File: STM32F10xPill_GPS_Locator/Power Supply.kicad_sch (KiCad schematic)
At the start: 42 parts, among them J3 Conn_01x02, Q1 2301D, U2 MCP73871T-2CCI/ML, U3 TPS61022RWUR

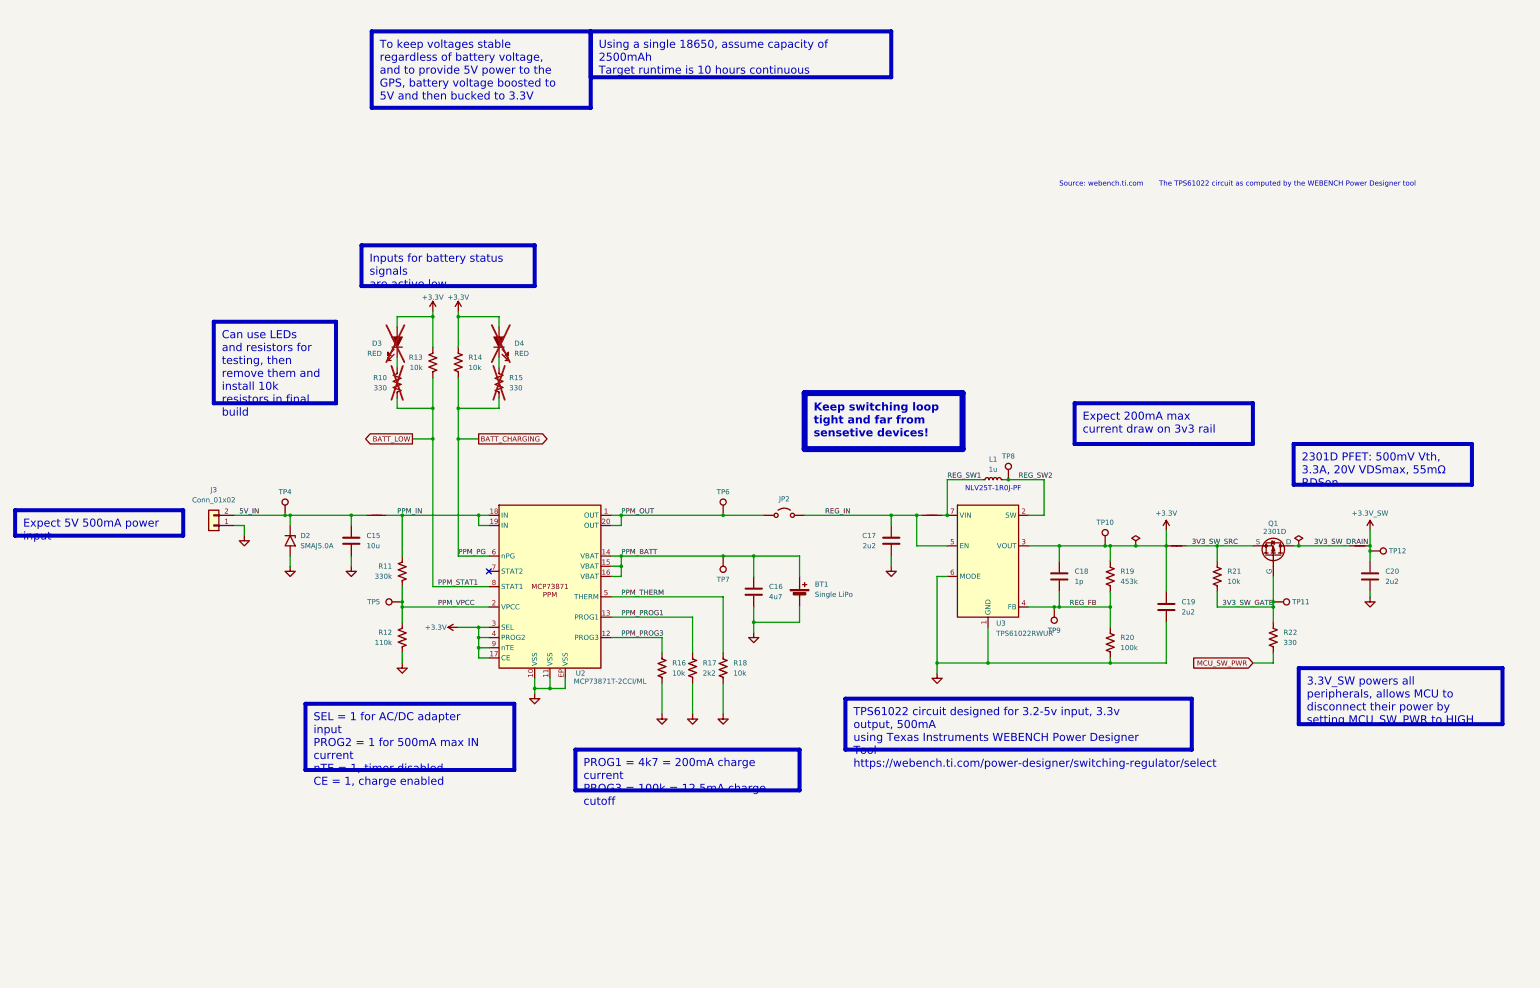
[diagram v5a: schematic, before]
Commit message: Add USB Port
Added schematic for controlling SEL and PROG2 on the PPM, as well as USB filtering and ESD protection and stuff. The board layout was not changed yet
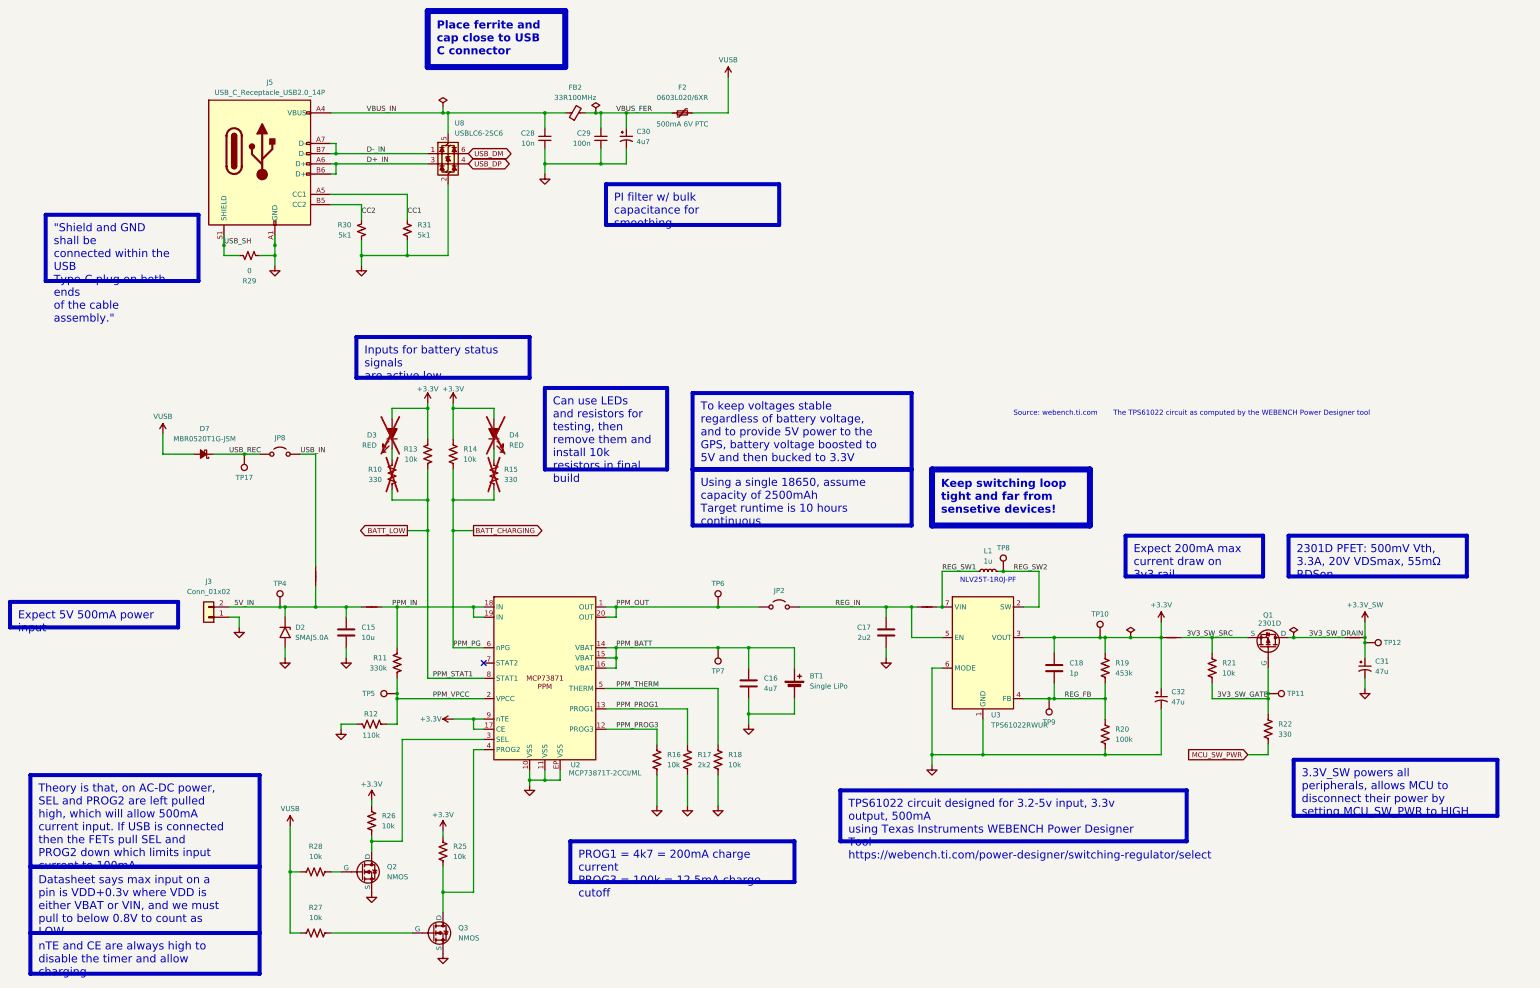
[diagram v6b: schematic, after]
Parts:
- removed C19, C20: 2u2, Capacitor_SMD:C_0603_1608Metric, symbol Device:C
- added C28: 10n, Capacitor_SMD:C_0402_1005Metric, symbol Device:C_Small
- added C29: 100n, Capacitor_SMD:C_0402_1005Metric, symbol Device:C_Small
- added C30: 4u7, Capacitor_SMD:CP_Elec_4x5.4, symbol Device:C_Polarized_Small_US
- added C31, C32: 47u, Capacitor_SMD:CP_Elec_4x5.4, symbol Device:C_Polarized_Small_US
- added D7: MBR0520T1G-JSM, Diode_SMD:D_SOD-123, symbol Device:D_Schottky_Small_Filled
- added F2: 0603L020/6XR, Fuse:Fuse_0603_1608Metric_Pad1.05x0.95mm_HandSolder, symbol Device:Polyfuse_Small
- added FB2: 33R100MHz, Inductor_SMD:L_0402_1005Metric, symbol Device:FerriteBead_Small
- added J5: USB_C_Receptacle_USB2.0_14P, Connector_USB:USB_C_Receptacle_HRO_TYPE-C-31-M-12, symbol Connector:USB_C_Receptacle_USB2.0_14P
- added JP8: Jumper_2_Open, Jumper:SolderJumper-2_P1.3mm_Open_Pad1.0x1.5mm, symbol Jumper:Jumper_2_Open
- added NT6: NetTie_2, NetTie:NetTie-2_SMD_Pad0.5mm, symbol Device:NetTie_2
- added Q2, Q3: NMOS, symbol Simulation_SPICE:NMOS
- added R25, R26, R27, R28: 10k, Resistor_SMD:R_0402_1005Metric_Pad0.72x0.64mm_HandSolder, symbol Device:R_US
- added R29: 0, Resistor_SMD:R_0402_1005Metric, symbol Device:R_Small_US
- added R30, R31: 5k1, Resistor_SMD:R_0402_1005Metric, symbol Device:R_Small_US
- added TP17: USB_REC, TestPoint:TestPoint_Pad_D1.5mm, symbol Connector:TestPoint
- added U8: USBLC6-2SC6, Package_TO_SOT_SMD:SOT-23-6, symbol Power_Protection:USBLC6-2SC6
- TP4: value PPM_IN -> 5V_IN
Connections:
- net +3.3V: now also C32.1, R25.2, R26.2; no longer U2.3 (SEL), U2.4 (PROG2)
- net +3.3V_SW: now also C31.1
- net 5V_IN: now also NT6.1
- net GND: now also R12.2, C28.1, C29.1, C30.2, C31.2, C32.2, J5.A1 (GND), J5.A12 (GND), J5.B1 (GND), J5.B12 (GND), Q2.3 (S), Q3.3 (S), R29.2, R30.1, R31.1, U8.2 (GND); no longer R12.1
- net PPM_VPCC: now also R12.1; no longer R12.2
- new net: Q2.1 (D), R26.1, U2.3 (SEL)
- new net: Q2.2 (G), R28.1
- new net: Q3.2 (G), R27.1
- new net: Q3.1 (D), R25.1, U2.4 (PROG2)
- new net CC1: J5.A5 (CC1), R31.2
- new net CC2: J5.B5 (CC2), R30.2
- new net D+_IN: J5.A6 (D+), J5.B6 (D+), U8.3 (I/O2)
- new net D-_IN: J5.A7 (D-), J5.B7 (D-), U8.1 (I/O1)
- new net USB_DM: U8.6 (I/O1)
- new net USB_DP: U8.4 (I/O2)
- new net USB_IN: JP8.2 (B), NT6.2
- new net USB_REC: D7.1 (K), JP8.1 (A), TP17.1
- new net USB_SH: J5.S1 (SHIELD), R29.1
- new net VBUS_FER: C29.2, C30.1, F2.1, FB2.2
- new net VBUS_IN: C28.2, FB2.1, J5.A4 (VBUS), J5.A9 (VBUS), J5.B4 (VBUS), J5.B9 (VBUS), U8.5 (VBUS)
- new net VUSB: D7.2 (A), F2.2, R27.2, R28.2
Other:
- moved on the sheet: BT1, C15, C16, C17, C18, D2, D3, D4, J3, JP2, L1, Q1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

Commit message: Added SD card and updated PCB layout
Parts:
- C31, C32: value 47u -> 10u
- J5: value USB_C_Receptacle_USB2.0_14P -> TYPE-C-31-M-12; LCSC Part (none) -> C165948
- Q2, Q3: value NMOS -> 2SK3019-ES; footprint (none) -> Package_TO_SOT_SMD:SOT-523; LCSC Part (none) -> 2SK3019-ES
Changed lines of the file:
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@@
 			)
 		)
-		(property "Value" "NMOS"
+		(property "Value" "2SK3019-ES"
 			(at 119.38 240.03 0)
 			(effects
@@
 			)
 		)
-		(property "Footprint" ""
+		(property "Footprint" "Package_TO_SOT_SMD:SOT-523"
 			(at 118.11 236.22 0)
 			(effects
@@
 			)
 		)
+		(property "LCSC Part" "2SK3019-ES"
+			(at 113.03 238.76 0)
+			(effects
+				(font
+					(size 1.27 1.27)
+				)
+				(hide yes)
+			)
+		)
 		(pin "2"
 		)
@@
 	)
 	(symbol
+		(lib_id "Simulation_SPICE:NMOS")
+		(at 130.81 254 0)
+		(unit 1)
+		(exclude_from_sim no)
+		(in_bom yes)
+		(on_board yes)
+		(dnp no)
+		(fields_autoplaced yes)
+		(property "Reference" "Q3"
+			(at 137.16 252.73 0)
+			(effects
+				(font
+					(size 1.27 1.27)
+				)
+				(justify left)
+			)
+		)
+		(property "Value" "2SK3019-ES"
+			(at 137.16 255.27 0)
+			(effects
+				(font
+					(size 1.27 1.27)
+				)
+				(justify left)
+			)
+		)
+		(property "Footprint" "Package_TO_SOT_SMD:SOT-523"
+			(at 135.89 251.46 0)
+			(effects
+				(font
+					(size 1.27 1.27)
+				)
+				(hide yes)
+			)
+		)
+		(property "Datasheet" "https://ngspice.sourceforge.io/docs/ngspice-html-manual/manual.xhtml#cha_MOSFETs"
+			(at 130.81 266.7 0)
+			(effects
+				(font
+					(size 1.27 1.27)
+				)
+				(hide yes)
+			)
+		)
+		(property "Description" "N-MOSFET transistor, drain/source/gate"
+			(at 130.81 254 0)
+			(effects
+				(font
+					(size 1.27 1.27)
+				)
+				(hide yes)
+			)
+		)
+		(property "Sim.Device" "NMOS"
+			(at 130.81 271.145 0)
+			(effects
+				(font
+					(size 1.27 1.27)
+				)
+				(hide yes)
+			)
+		)
+		(property "Sim.Type" "VDMOS"
+			(at 130.81 273.05 0)
+			(effects
+				(font
+					(size 1.27 1.27)
+				)
+				(hide yes)
+			)
+		)
+		(property "Sim.Pins" "1=D 2=G 3=S"
+			(at 130.81 269.24 0)
+			(effects
+				(font
+					(size 1.27 1.27)
+				)
+				(hide yes)
+			)
+		)
+		(property "LCSC Part" "2SK3019-ES"
+			(at 130.81 254 0)
+			(effects
+				(font
+					(size 1.27 1.27)
+				)
+				(hide yes)
+			)
+		)
+		(pin "2"
+		)
+		(pin "1"
+		)
+		(pin "3"
+		)
+		(instances
+			(project "STM32F10xPill_GPS_Locator"
+				(path "/ea8b3ef8-8ecc-4b82-8187-a133f9b3c76f/bb542a6e-ba6f-4c6c-9344-4b3df55a7ad0"
+					(reference "Q3")
+					(unit 1)
+				)
+			)
+		)
+	)
+	(symbol
 		(lib_id "Device:C_Polarized_Small_US")
 		(at 312.42 195.58 0)
@@
 			)
 		)
-		(property "Value" "47u"
+		(property "Value" "10u"
 			(at 314.96 196.4181 0)
 			(effects
@@
 			)
 		)
-		(property "Value" "USB_C_Receptacle_USB2.0_14P"
+		(property "Value" "TYPE-C-31-M-12"
 			(at 90.17 44.45 0)
 			(effects
@@
 			)
 		)
+		(property "LCSC Part" "C165948"
+			(at 90.17 68.58 0)
+			(effects
+				(font
+					(size 1.27 1.27)
+				)
+				(hide yes)
+			)
+		)
 		(pin "B12"
 		)
@@
 	)
 	(symbol
-		(lib_id "Simulation_SPICE:NMOS")
-		(at 130.81 254 0)
-		(unit 1)
-		(exclude_from_sim no)
-		(in_bom yes)
-		(on_board yes)
-		(dnp no)
-		(fields_autoplaced yes)
-		(property "Reference" "Q3"
-			(at 137.16 252.73 0)
-			(effects
-				(font
-					(size 1.27 1.27)
-				)
-				(justify left)
-			)
-		)
-		(property "Value" "NMOS"
-			(at 137.16 255.27 0)
-			(effects
-				(font
-					(size 1.27 1.27)
-				)
-				(justify left)
-			)
-		)
-		(property "Footprint" ""
-			(at 135.89 251.46 0)
-			(effects
-				(font
-					(size 1.27 1.27)
-				)
-				(hide yes)
-			)
-		)
-		(property "Datasheet" "https://ngspice.sourceforge.io/docs/ngspice-html-manual/manual.xhtml#cha_MOSFETs"
-			(at 130.81 266.7 0)
-			(effects
-				(font
-					(size 1.27 1.27)
-				)
-				(hide yes)
-			)
-		)
-		(property "Description" "N-MOSFET transistor, drain/source/gate"
-			(at 130.81 254 0)
-			(effects
-				(font
-					(size 1.27 1.27)
-				)
-				(hide yes)
-			)
-		)
-		(property "Sim.Device" "NMOS"
-			(at 130.81 271.145 0)
-			(effects
-				(font
-					(size 1.27 1.27)
-				)
-				(hide yes)
-			)
-		)
-		(property "Sim.Type" "VDMOS"
-			(at 130.81 273.05 0)
-			(effects
-				(font
-					(size 1.27 1.27)
-				)
-				(hide yes)
-			)
-		)
-		(property "Sim.Pins" "1=D 2=G 3=S"
-			(at 130.81 269.24 0)
-			(effects
-				(font
-					(size 1.27 1.27)
-				)
-				(hide yes)
-			)
-		)
-		(pin "2"
-		)
-		(pin "1"
-		)
-		(pin "3"
-		)
-		(instances
-			(project "STM32F10xPill_GPS_Locator"
-				(path "/ea8b3ef8-8ecc-4b82-8187-a133f9b3c76f/bb542a6e-ba6f-4c6c-9344-4b3df55a7ad0"
-					(reference "Q3")
-					(unit 1)
-				)
-			)
-		)
-	)
-	(symbol
 		(lib_id "power:GND")
 		(at 255.27 212.09 0)
@@
 			)
 		)
-		(property "Value" "47u"
+		(property "Value" "10u"
 			(at 365.76 188.7981 0)
 			(effects
